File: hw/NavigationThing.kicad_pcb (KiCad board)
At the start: 2 copper layers, 64 x 58 mm, 35 parts, among them P1 CONN_01X02, SW1 SW_PUSH, U1 HMC5983_module, U2 arduino_nano, U3 PIEZO, U4 NEO-6M_module

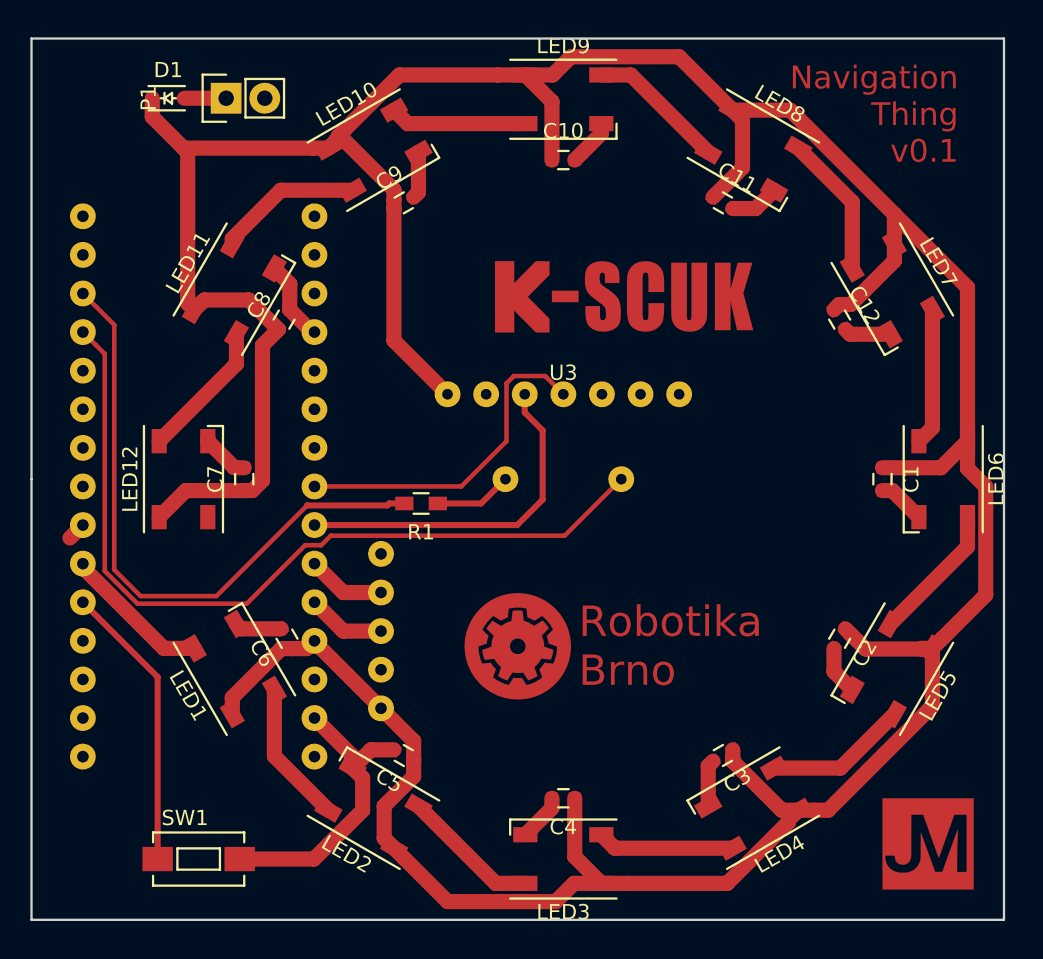
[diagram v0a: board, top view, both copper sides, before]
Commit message: New board version
- change GPS pins, as the original ones were purely ADC
- move piezo a little bit to make space for GPS antenna
- add hole for GPS antenna
- change signature to text instead of logo (which does not render in SVG)
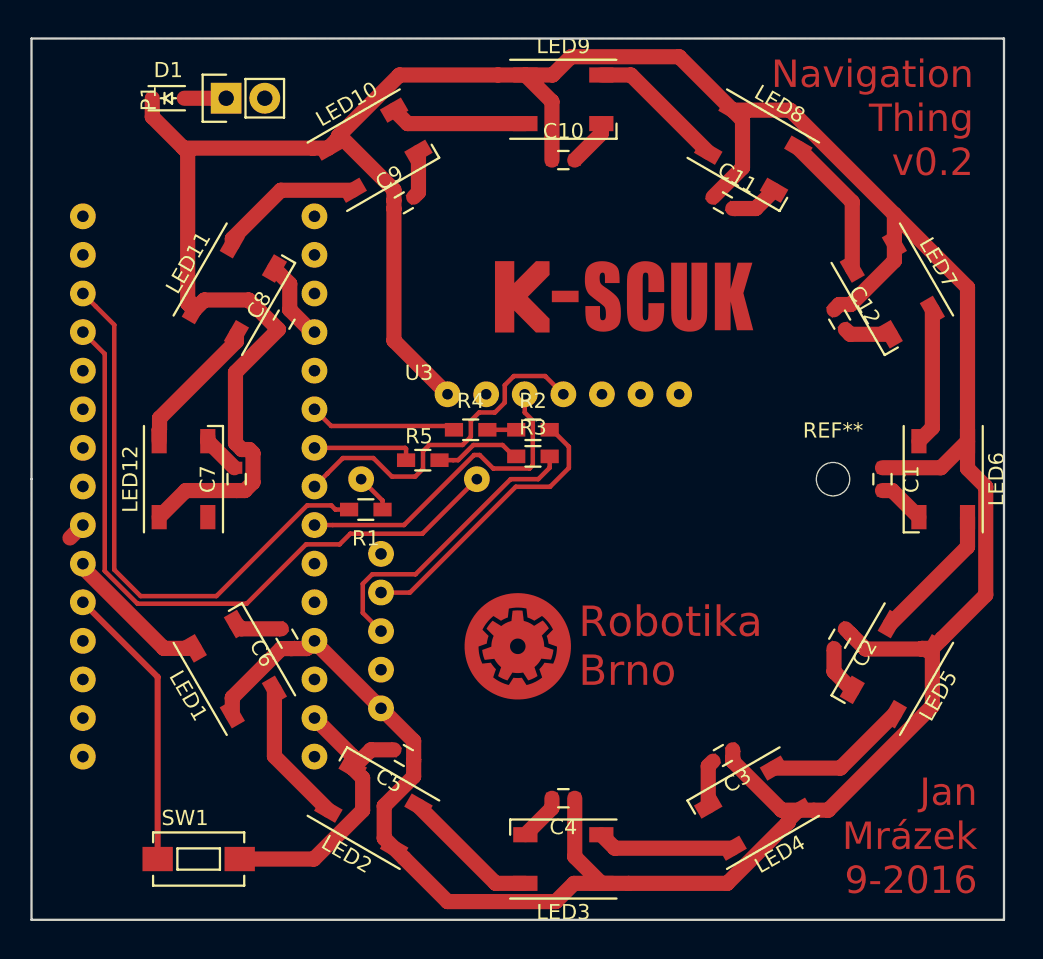
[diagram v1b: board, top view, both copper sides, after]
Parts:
- removed G***: LOGO, yaqwsx:JM_6
- added R2: 0R, Resistors_SMD:R_0603_HandSoldering, F.Cu at (151.0, 96.8)
- added R3: 0R, Resistors_SMD:R_0603_HandSoldering, F.Cu at (151.0, 98.5)
- added R4: 0R, Resistors_SMD:R_0603_HandSoldering, F.Cu at (146.9, 96.8)
- added R5: 0R, Resistors_SMD:R_0603_HandSoldering, F.Cu at (143.8, 98.8)
- added REF**: MountingHole_2.2mm_M2, Mounting_Holes:MountingHole_2.2mm_M2, F.Cu at (170.8, 100.0)
- moved U3 9.50 mm to (143.5, 100.0)
- moved R1 3.66 mm to (140.0, 102.0)
- moved C7 0.50 mm to (131.5, 100.0)
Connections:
- LED12 pad 2: Net-(LED12-Pad2) -> (no net)
- U1 pad 5: Net-(U1-Pad5) -> (no net)
- U1 pad 6: Net-(U1-Pad6) -> (no net)
- U1 pad 7: Net-(U1-Pad7) -> (no net)
- U2 pad 1: Net-(U2-Pad1) -> (no net)
- U2 pad 10: Net-(U2-Pad10) -> GND
- U2 pad 11: Net-(U2-Pad11) -> GND
- U2 pad 13: Net-(U2-Pad13) -> (no net)
- U2 pad 15: Net-(U2-Pad15) -> (no net)
- U2 pad 16: Net-(U2-Pad16) -> (no net)
- U2 pad 17: Net-(U2-Pad17) -> (no net)
- U2 pad 18: Net-(U2-Pad18) -> (no net)
- U2 pad 2: Net-(U2-Pad2) -> (no net)
- U2 pad 29: Net-(U2-Pad29) -> (no net)
- U2 pad 3: Net-(U2-Pad3) -> (no net)
- U2 pad 30: Net-(U2-Pad30) -> (no net)
- U2 pad 6: GND -> Net-(R4-Pad1)
- U2 pad 7: GND -> Net-(R5-Pad1)
- U4 pad 1: Net-(U4-Pad1) -> (no net)
- U4 pad 2: Net-(U2-Pad10) -> Net-(R2-Pad2)
- U4 pad 3: Net-(U2-Pad11) -> Net-(R3-Pad2)
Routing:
- net Net-(R3-Pad2): track 0.00 -> 19.8 mm
- net Net-(R2-Pad2): track 0.00 -> 18.9 mm
- net Net-(R4-Pad1): track 0.00 -> 9.64 mm
- net Net-(U2-Pad27): track 54.6 -> 45.1 mm
- net Net-(R5-Pad1): track 0.00 -> 6.80 mm
- net Net-(R3-Pad1): track 0.00 -> 5.77 mm
- net Net-(U2-Pad11): track 5.17 -> 0.00 mm
- net Net-(U2-Pad10): track 5.17 -> 0.00 mm
- net Net-(R1-Pad2): track 41.4 -> 37.8 mm
- net Net-(R1-Pad1): track 5.12 -> 2.58 mm
- net Net-(R2-Pad1): track 0.00 -> 1.90 mm
- net Net-(U1-Pad3): track 23.1 -> 21.6 mm
- net +5V: track 264.7 -> 265.6 mm
- net Net-(U1-Pad4): track 22.1 -> 22.9 mm
- net GND: track 58.2 -> 57.5 mm
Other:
- net class Default: trace_width 0.4 -> 0.3
- board text added: "Jan Mrázek 9-2016"
- board text added: "Navigation Thing v0.2"
- board text removed: "Navigation Thing v0.1"

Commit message: Small board adjustements
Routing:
- net GND: track 57.5 -> 50.8 mm
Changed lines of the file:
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@@
   (general
     (links 90)
-    (no_connects 6)
-    (area 117.924999 70.924999 182.075001 129.075001)
+    (no_connects 0)
+    (area 117.924999 69.896666 182.575 129.575)
     (thickness 1.6)
     (drawings 8)
-    (tracks 241)
+    (tracks 240)
     (zones 0)
     (modules 39)
@@
     (46 B.CrtYd user)
     (47 F.CrtYd user)
-    (48 B.Fab user hide)
+    (48 B.Fab user)
     (49 F.Fab user)
   )
@@
     (visible_elements FFFFFF7F)
     (pcbplotparams
-      (layerselection 0x00030_80000001)
+      (layerselection 0x00000_00000001)
       (usegerberextensions false)
-      (excludeedgelayer true)
+      (excludeedgelayer false)
       (linewidth 0.100000)
       (plotframeref false)
@@
       (psnegative false)
       (psa4output false)
-      (plotreference true)
-      (plotvalue true)
+      (plotreference false)
+      (plotvalue false)
       (plotinvisibletext false)
       (padsonsilk false)
       (subtractmaskfromsilk false)
-      (outputformat 1)
-      (mirror false)
+      (outputformat 5)
+      (mirror true)
       (drillshape 1)
       (scaleselection 1)
@@
   (gr_line (start 118 71) (end 182 71) (layer Edge.Cuts) (width 0.15))
   (gr_line (start 118 100) (end 118 71) (layer Edge.Cuts) (width 0.15))
+  (segment (start 138.191286 77.557373) (end 138.191286 77.22569) (width 1) (layer F.Cu) (net 1))
+  (segment (start 138.191286 77.22569) (end 142.016976 73.4) (width 1) (layer F.Cu) (net 1))
+  (segment (start 142.016976 73.4) (end 148.7 73.4) (width 1) (layer F.Cu) (net 1))
+  (segment (start 148.7 73.4) (end 150.5 73.4) (width 1) (layer F.Cu) (net 1))
+  (segment (start 164.134936 75.713723) (end 160.579924 72.158711) (width 1) (layer F.Cu) (net 1))
+  (segment (start 160.579924 72.158711) (end 153.541289 72.158711) (width 1) (layer F.Cu) (net 1))
+  (segment (start 153.541289 72.158711) (end 152.3 73.4) (width 1) (layer F.Cu) (net 1))
+  (segment (start 152.3 73.4) (end 150.5 73.4) (width 1) (layer F.Cu) (net 1))
+  (segment (start 174.786276 82.569138) (end 174.786276 82.364113) (width 1) (layer F.Cu) (net 1))
+  (segment (start 174.786276 82.364113) (end 168.135886 75.713723) (width 1) (layer F.Cu) (net 1))
+  (segment (start 168.135886 75.713723) (end 165.158695 75.713723) (width 1) (layer F.Cu) (net 1))
+  (segment (start 165.158695 75.713723) (end 164.134936 75.713723) (width 1) (layer F.Cu) (net 1))
   (segment (start 131.5 100.75) (end 128.15 100.75) (width 1) (layer F.Cu) (net 1))
   (segment (start 131.84706 98.04999) (end 132.334992 98.04999) (width 1) (layer F.Cu) (net 1))
@@
   (segment (start 180.80001 107.621202) (end 177.942626 110.478586) (width 1) (layer F.Cu) (net 1))
   (segment (start 177.942626 110.478586) (end 177.286276 111.134936) (width 1) (layer F.Cu) (net 1))
-  (segment (start 164.134936 75.713723) (end 160.621204 72.199991) (width 1) (layer F.Cu) (net 1))
-  (segment (start 160.621204 72.199991) (end 153.500009 72.199991) (width 1) (layer F.Cu) (net 1))
-  (segment (start 153.500009 72.199991) (end 152.3 73.4) (width 1) (layer F.Cu) (net 1))
-  (segment (start 152.3 73.4) (end 150.5 73.4) (width 1) (layer F.Cu) (net 1))
   (segment (start 179.6 97.5) (end 179.6 87.382862) (width 1) (layer F.Cu) (net 1))
   (segment (start 179.6 87.382862) (end 174.786276 82.569138) (width 1) (layer F.Cu) (net 1))
@@
   (segment (start 174.786276 85.62945) (end 174.786276 85.558694) (width 1) (layer F.Cu) (net 1))
   (segment (start 174.786276 84.534935) (end 174.786276 82.569138) (width 1) (layer F.Cu) (net 1))
-  (segment (start 174.786276 82.569138) (end 167.930861 75.713723) (width 1) (layer F.Cu) (net 1))
-  (segment (start 167.930861 75.713723) (end 165.158695 75.713723) (width 1) (layer F.Cu) (net 1))
-  (segment (start 165.158695 75.713723) (end 164.134936 75.713723) (width 1) (layer F.Cu) (net 1))
   (segment (start 162.850481 81.438466) (end 164.791286 79.497661) (width 1) (layer F.Cu) (net 1))
   (segment (start 164.791286 79.497661) (end 164.791286 76.370073) (width 1) (layer F.Cu) (net 1))
@@
   (segment (start 141.850481 81.655453) (end 141.850481 82.188466) (width 1) (layer F.Cu) (net 1))
   (segment (start 137.534936 78.213723) (end 138.191286 77.557373) (width 1) (layer F.Cu) (net 1))
-  (segment (start 138.191286 77.557373) (end 138.191286 77.421704) (width 1) (layer F.Cu) (net 1))
-  (segment (start 138.191286 77.421704) (end 142.21299 73.4) (width 1) (layer F.Cu) (net 1))
-  (segment (start 142.21299 73.4) (end 148.7 73.4) (width 1) (layer F.Cu) (net 1))
-  (segment (start 148.7 73.4) (end 150.5 73.4) (width 1) (layer F.Cu) (net 1))
   (segment (start 155.5 126.6) (end 155.2 126.6) (width 1) (layer F.Cu) (net 1))
   (segment (start 120.530001 103.869999) (end 121.38 103.02) (width 1) (layer F.Cu) (net 2))
@@
   (segment (start 131.80055 109.850481) (end 131.485005 109.534936) (width 1) (layer F.Cu) (net 2))
   (segment (start 131.7 125) (end 136.587009 125) (width 1) (layer F.Cu) (net 2))
-  (segment (start 136.587009 125) (end 139.791286 121.795723) (width 1) (layer F.Cu) (net 2))
-  (segment (start 139.791286 121.795723) (end 139.791286 119.671344) (width 1) (layer F.Cu) (net 2))
   (segment (start 139.791286 119.671344) (end 139.134936 119.014994) (width 1) (layer F.Cu) (net 2))
   (segment (start 136.62 115.72) (end 139.134936 118.234936) (width 1) (layer F.Cu) (net 2))
